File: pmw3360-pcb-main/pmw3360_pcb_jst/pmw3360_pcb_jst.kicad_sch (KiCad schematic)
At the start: 20 parts, among them J1 Conn_01x08, U1 PMW3360DM-T2QU, U2 TLV74318PDBVR

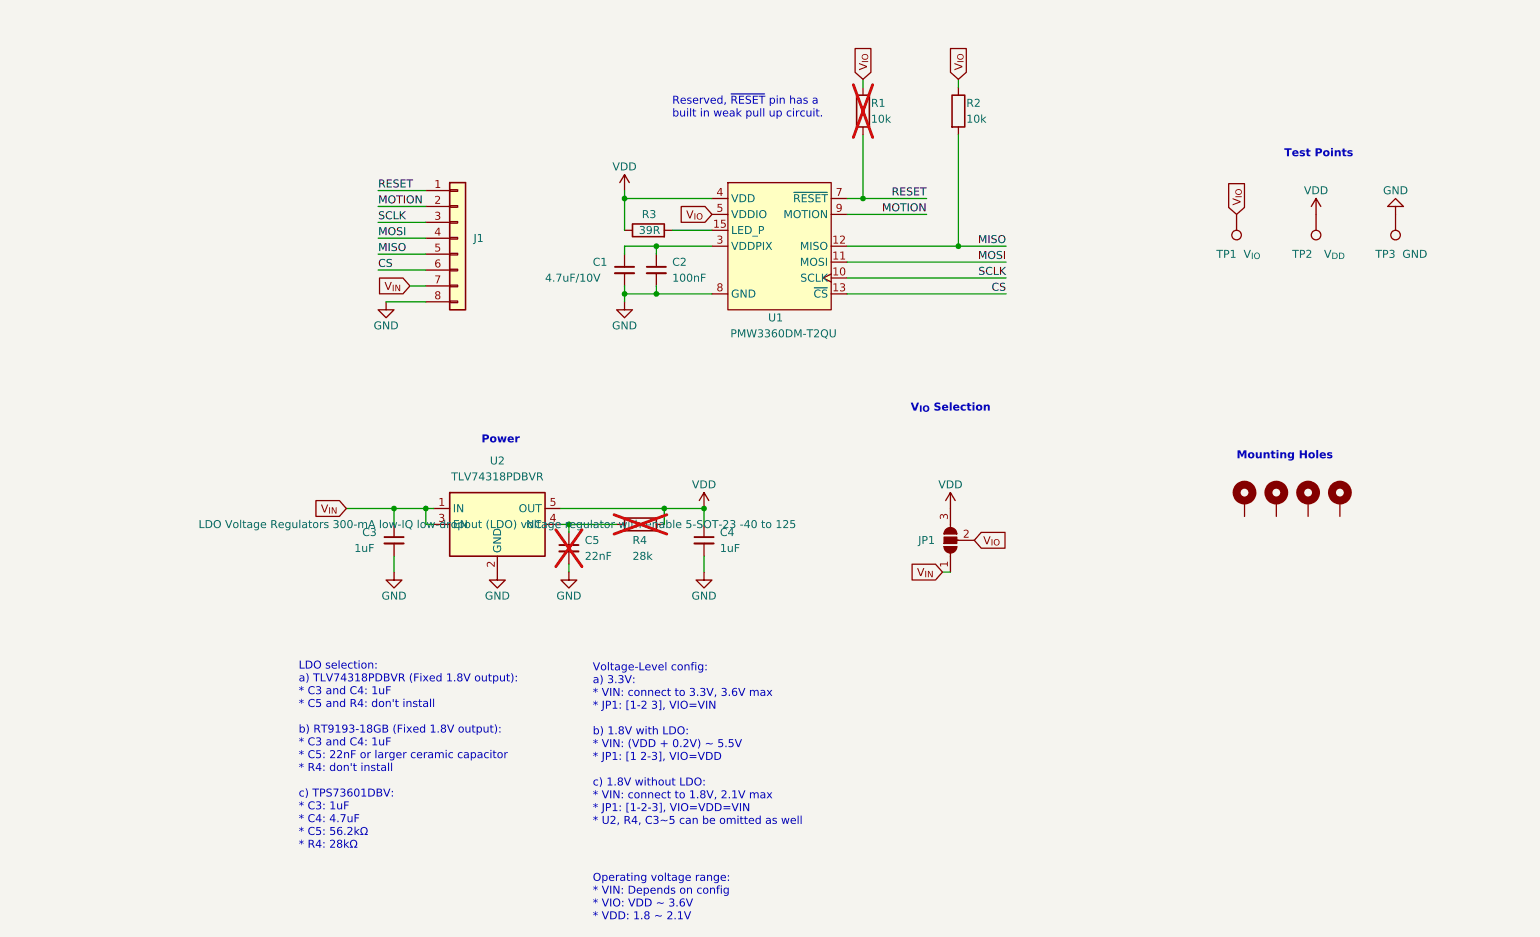
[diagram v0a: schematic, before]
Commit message: mouse sensor bots libraries
- footprints not done yet. shematics yes.
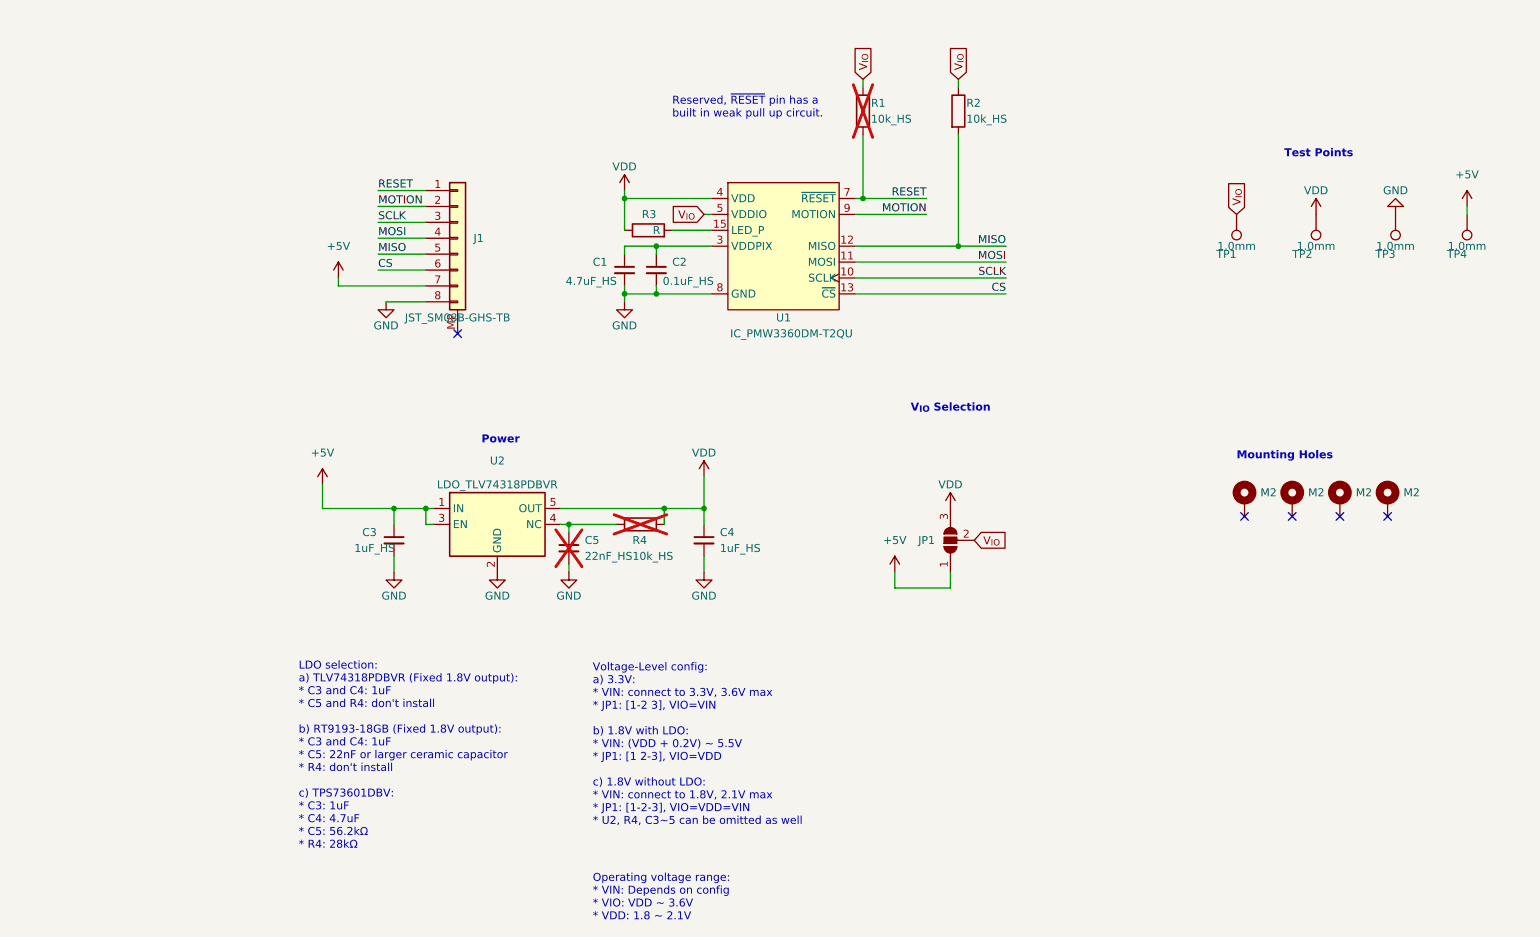
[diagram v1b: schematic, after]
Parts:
- added TP4: 1.0mm, TestPoint:TestPoint_Pad_D1.0mm, symbol bots:TestPoint1.0mm
- C1: value 4.7uF/10V -> 4.7uF_HS; symbol Device:C_Small -> bots:C_4.7uF_HS
- C2: value 100nF -> 0.1uF_HS; symbol Device:C_Small -> bots:C_0.1uF_HS
- C3, C4: value 1uF -> 1uF_HS; symbol Device:C_Small -> bots:C_1uF_HS
- C5: value 22nF -> 22nF_HS; symbol Device:C_Small -> bots:C_22nF_HS; MPN (none) -> CL10B223KB8NNNC; Mfr. # CL10B223KB8NNNC -> (none)
- H1, H2, H3, H4: value MountingHole_Pad -> M2; footprint MountingHole:MountingHole_2.2mm_M2_ISO14580_Pad -> bots:MountingHole_2.2mm_M2_ISO14580_Pad; symbol Mechanical:MountingHole_Pad -> bots:MountingHole_Pad_M2NoThread
- J1: value Conn_01x08 -> JST_SM08B-GHS-TB; symbol Connector_Generic:Conn_01x08 -> bots:JST_SM08B-GHS-TB
- JP1: symbol Jumper:SolderJumper_3_Open -> bots:SolderJumper_3_Open; now left out of the parts list
- R1, R2: value 10k -> 10k_HS; symbol Device:R -> bots:R_10k_HS
- R3: value 39R -> R
- R4: value 28k -> 10k_HS; symbol Device:R -> bots:R_10k_HS
- TP1: value V_{IO} -> 1.0mm; symbol Connector:TestPoint -> bots:TestPoint1.0mm
- TP2: value V_{DD} -> 1.0mm; symbol Connector:TestPoint -> bots:TestPoint1.0mm
- TP3: value GND -> 1.0mm; symbol Connector:TestPoint -> bots:TestPoint1.0mm
- U1: value PMW3360DM-T2QU -> IC_PMW3360DM-T2QU; footprint PMW3360_PCB:PMW3360DM-T2QU 16Pin -> bots:IC_PMW3360DM-T2QU 16Pin; symbol PMW3360_PCB:PMW3360DM-T2QU -> bots:IC_PMW3360DM-T2QU
- U2: value TLV74318PDBVR -> LDO_TLV74318PDBVR; symbol PMW3360_PCB:TLV74318PDBVR -> bots:LDO_TLV74318PDBVR
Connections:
- net V_{IN} renamed +5V
- net +5V: now also TP4.1
- no-connect marks 0 -> 5
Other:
- moved on the sheet: U1

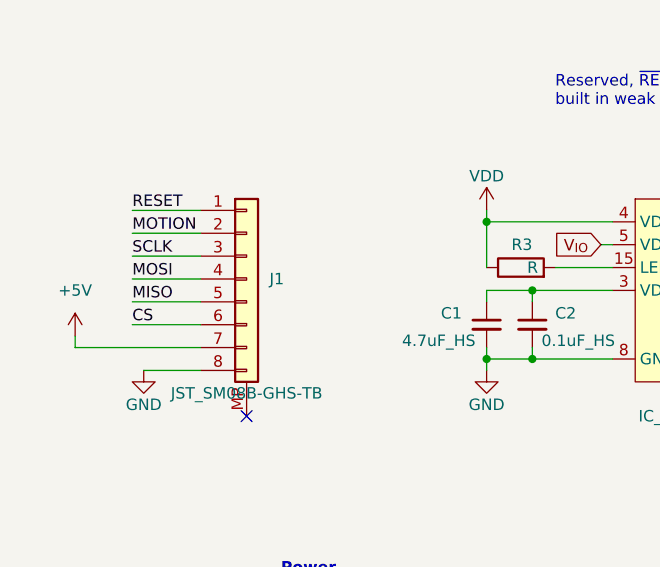
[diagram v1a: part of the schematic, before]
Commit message: 3dmodels + footprints
- one resistor unvalued + no footprint
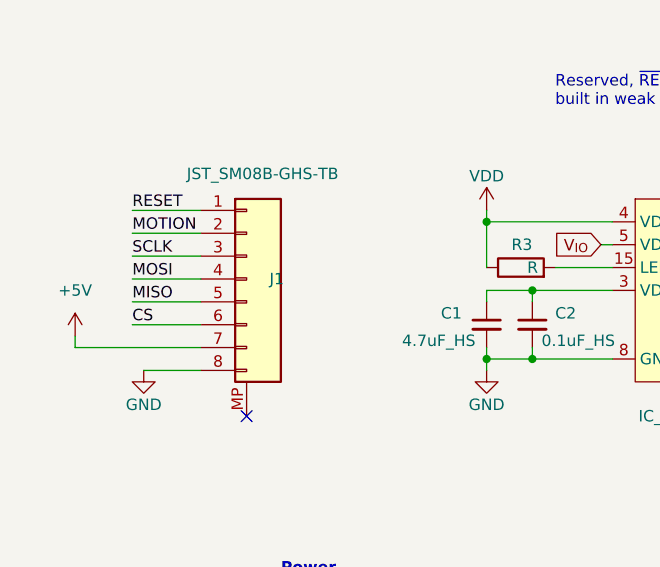
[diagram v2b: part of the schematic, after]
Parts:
- C1, C2, C3, C4, C5: footprint Capacitor_SMD:C_0603_1608Metric_Pad1.08x0.95mm_HandSolder -> bots:C_0603_1608Metric_Pad1.08x0.95mm_HandSolder
- J1: footprint Connector_JST:JST_GH_SM08B-GHS-TB_1x08-1MP_P1.25mm_Horizontal -> bots:JST_GH_SM08B-GHS-TB_1x08-1MP_P1.25mm_Horizontal
- JP1: footprint Jumper:SolderJumper-3_P1.3mm_Open_RoundedPad1.0x1.5mm_NumberLabels -> bots:SolderJumper-3_P1.3mm_Open_RoundedPad1.0x1.5mm_NumberLabels
- R1, R2, R4: footprint Resistor_SMD:R_0603_1608Metric_Pad0.98x0.95mm_HandSolder -> bots:R_0603_1608Metric_Pad0.98x0.95mm_HandSolder
- R3: footprint Resistor_SMD:R_0603_1608Metric_Pad0.98x0.95mm_HandSolder -> (none)
- TP1, TP2, TP3, TP4: footprint TestPoint:TestPoint_Pad_D1.0mm -> bots:TestPoint_Pad_D1.0mm
- U2: LCSC C485152 -> (none); Mfr. # TLV74318PDBVR -> (none)
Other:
- moved on the sheet: J1
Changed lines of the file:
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@@
 			)
 		)
-		(property "Footprint" "TestPoint:TestPoint_Pad_D1.0mm"
+		(property "Footprint" "bots:TestPoint_Pad_D1.0mm"
 			(at 222.25 71.12 0)
 			(effects
@@
 			)
 		)
-		(property "Footprint" "Resistor_SMD:R_0603_1608Metric_Pad0.98x0.95mm_HandSolder"
+		(property "Footprint" "bots:R_0603_1608Metric_Pad0.98x0.95mm_HandSolder"
 			(at 119.38 118.872 90)
 			(effects
@@
 			)
 		)
-		(property "Footprint" "Capacitor_SMD:C_0603_1608Metric_Pad1.08x0.95mm_HandSolder"
+		(property "Footprint" "bots:C_0603_1608Metric_Pad1.08x0.95mm_HandSolder"
 			(at 129.54 123.19 0)
 			(effects
@@
 			)
 		)
-		(property "Footprint" "Resistor_SMD:R_0603_1608Metric_Pad0.98x0.95mm_HandSolder"
+		(property "Footprint" ""
 			(at 120.65 75.438 90)
 			(effects
@@
 			)
 		)
-		(property "Footprint" "Capacitor_SMD:C_0603_1608Metric_Pad1.08x0.95mm_HandSolder"
+		(property "Footprint" "bots:C_0603_1608Metric_Pad1.08x0.95mm_HandSolder"
 			(at 116.84 80.01 0)
 			(effects
@@
 			)
 		)
-		(property "Footprint" "Capacitor_SMD:C_0603_1608Metric_Pad1.08x0.95mm_HandSolder"
+		(property "Footprint" "bots:C_0603_1608Metric_Pad1.08x0.95mm_HandSolder"
 			(at 107.95 124.46 0)
 			(effects
@@
 			)
 		)
-		(property "Footprint" "TestPoint:TestPoint_Pad_D1.0mm"
+		(property "Footprint" "bots:TestPoint_Pad_D1.0mm"
 			(at 246.38 71.12 0)
 			(effects
@@
 			)
 		)
-		(property "Footprint" "Capacitor_SMD:C_0603_1608Metric_Pad1.08x0.95mm_HandSolder"
+		(property "Footprint" "bots:C_0603_1608Metric_Pad1.08x0.95mm_HandSolder"
 			(at 80.01 123.19 0)
 			(effects
@@
 			)
 		)
-		(property "Footprint" "Resistor_SMD:R_0603_1608Metric_Pad0.98x0.95mm_HandSolder"
+		(property "Footprint" "bots:R_0603_1608Metric_Pad0.98x0.95mm_HandSolder"
 			(at 153.162 54.61 90)
 			(effects
@@
 			)
 		)
-		(property "Footprint" "Capacitor_SMD:C_0603_1608Metric_Pad1.08x0.95mm_HandSolder"
+		(property "Footprint" "bots:C_0603_1608Metric_Pad1.08x0.95mm_HandSolder"
 			(at 121.92 80.01 0)
 			(effects
@@
 			)
 		)
-		(property "Footprint" "TestPoint:TestPoint_Pad_D1.0mm"
+		(property "Footprint" "bots:TestPoint_Pad_D1.0mm"
 			(at 234.95 71.12 0)
 			(effects
@@
 			)
 		)
-		(property "Footprint" "Resistor_SMD:R_0603_1608Metric_Pad0.98x0.95mm_HandSolder"
+		(property "Footprint" "bots:R_0603_1608Metric_Pad0.98x0.95mm_HandSolder"
 			(at 168.402 54.61 90)
 			(effects
@@
 			)
 		)
-		(property "Footprint" "Jumper:SolderJumper-3_P1.3mm_Open_RoundedPad1.0x1.5mm_NumberLabels"
+		(property "Footprint" "bots:SolderJumper-3_P1.3mm_Open_RoundedPad1.0x1.5mm_NumberLabels"
 			(at 168.91 123.19 0)
 			(effects
@@
 			)
 		)
-		(property "LCSC" "C485152"
-			(at 96.52 120.65 0)
-			(effects
-				(font
-					(size 1.27 1.27)
-				)
-				(hide yes)
-			)
-		)
-		(property "Mfr. #" "TLV74318PDBVR"
-			(at 96.52 120.65 0)
-			(effects
-				(font
-					(size 1.27 1.27)
-				)
-				(hide yes)
-			)
-		)
 		(pin "1"
 		)
@@
 		)
 		(property "Value" "JST_SM08B-GHS-TB"
-			(at 90.17 87.63 0)
-			(effects
-				(font
-					(size 1.27 1.27)
-				)
-			)
-		)
-		(property "Footprint" "Connector_JST:JST_GH_SM08B-GHS-TB_1x08-1MP_P1.25mm_Horizontal"
+			(at 91.948 63.246 0)
+			(effects
+				(font
+					(size 1.27 1.27)
+				)
+			)
+		)
+		(property "Footprint" "bots:JST_GH_SM08B-GHS-TB_1x08-1MP_P1.25mm_Horizontal"
 			(at 90.17 74.93 0)
 			(effects
@@
 			)
 		)
-		(property "Footprint" "TestPoint:TestPoint_Pad_D1.0mm"
+		(property "Footprint" "bots:TestPoint_Pad_D1.0mm"
 			(at 209.55 71.12 0)
 			(effects

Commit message: libraries and stuff
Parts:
- R3: value R -> 39R_HS; footprint (none) -> bots:R_0603_1608Metric_Pad0.98x0.95mm_HandSolder; symbol Device:R -> bots:R_39R_HS
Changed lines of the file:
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@@
 	(text "V_{IO} Selection"
 		(exclude_from_sim no)
-		(at 162.56 102.87 0)
+		(at 163.322 108.458 0)
 		(effects
 			(font
@@
 	)
 	(symbol
-		(lib_id "Device:R")
+		(lib_id "bots:R_39R_HS")
 		(at 120.65 73.66 90)
 		(unit 1)
@@
 			)
 		)
-		(property "Value" "R"
-			(at 122.555 73.66 90)
+		(property "Value" "39R_HS"
+			(at 116.586 74.676 90)
 			(effects
 				(font
@@
 			)
 		)
-		(property "Footprint" ""
+		(property "Footprint" "bots:R_0603_1608Metric_Pad0.98x0.95mm_HandSolder"
 			(at 120.65 75.438 90)
 			(effects

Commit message: mouse_sensorV1 prod done
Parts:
- J1: value JST_SM08B-GHS-TB -> JST_BM08B-GHS-TBT; footprint bots:JST_GH_SM08B-GHS-TB_1x08-1MP_P1.25mm_Horizontal -> bots:JST_BM08B-GHS-TBT_LF__SN__N_; symbol bots:JST_SM08B-GHS-TB -> bots:JST_BM08B-GHS-TBT
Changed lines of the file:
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@@
 	)
 	(symbol
-		(lib_id "bots:JST_SM08B-GHS-TB")
+		(lib_id "bots:JST_BM08B-GHS-TBT")
 		(at 90.17 74.93 0)
 		(unit 1)
@@
 			)
 		)
-		(property "Value" "JST_SM08B-GHS-TB"
-			(at 91.948 63.246 0)
+		(property "Value" "JST_BM08B-GHS-TBT"
+			(at 92.71 92.202 0)
 			(effects
 				(font
@@
 			)
 		)
-		(property "Footprint" "bots:JST_GH_SM08B-GHS-TB_1x08-1MP_P1.25mm_Horizontal"
+		(property "Footprint" "bots:JST_BM08B-GHS-TBT_LF__SN__N_"
 			(at 90.17 74.93 0)
 			(effects

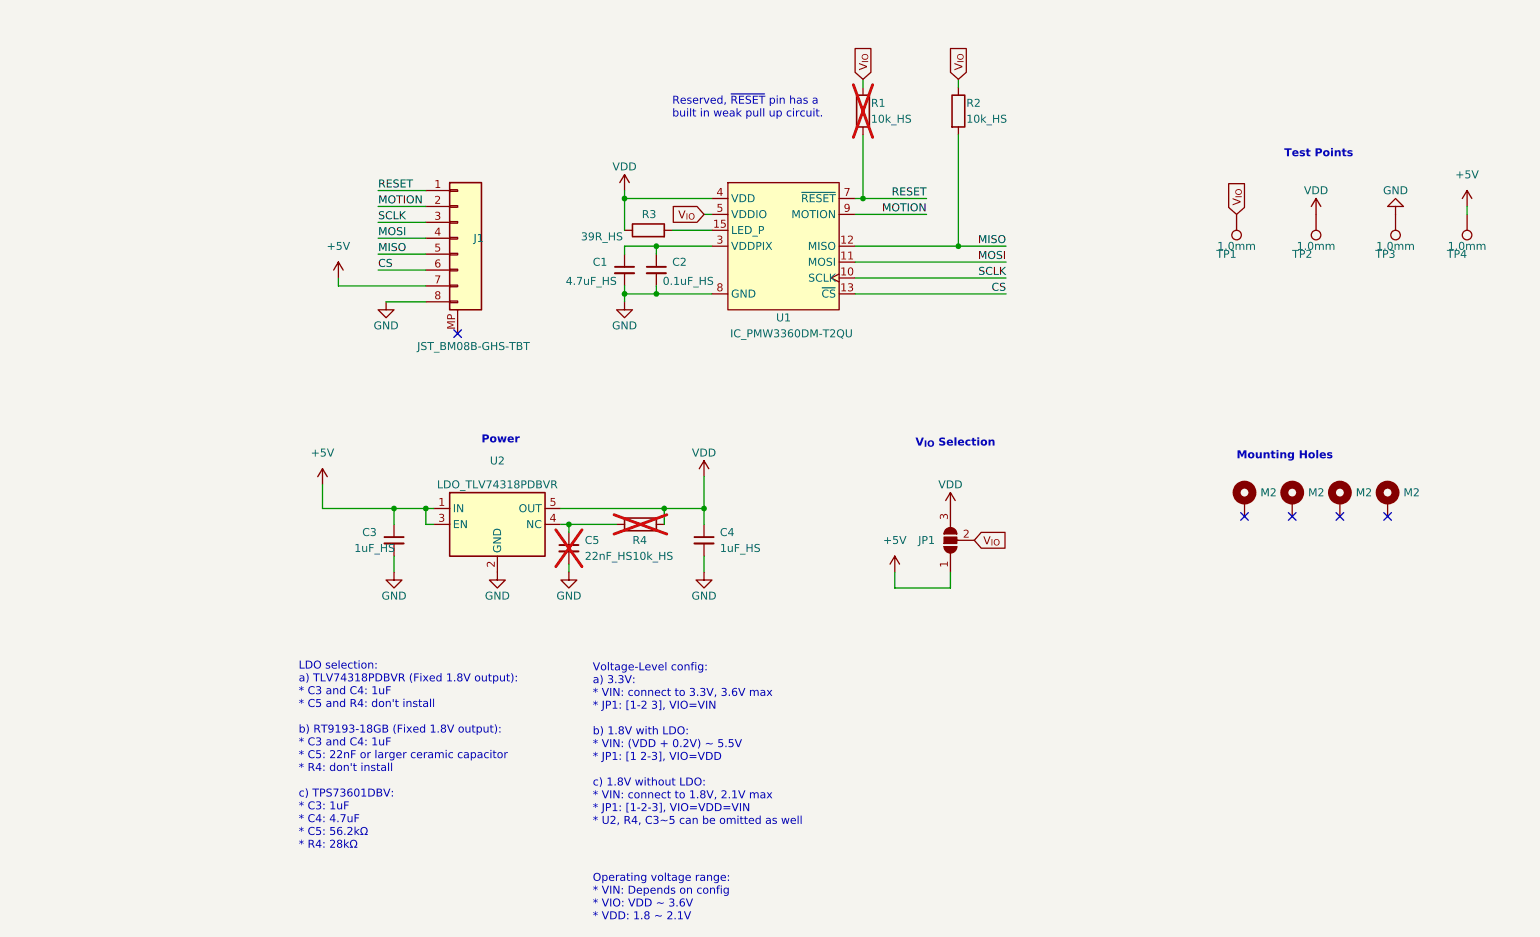
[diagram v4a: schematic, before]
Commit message: production files - working
- modified board slightly, added 3d models, added part numbers for JLC
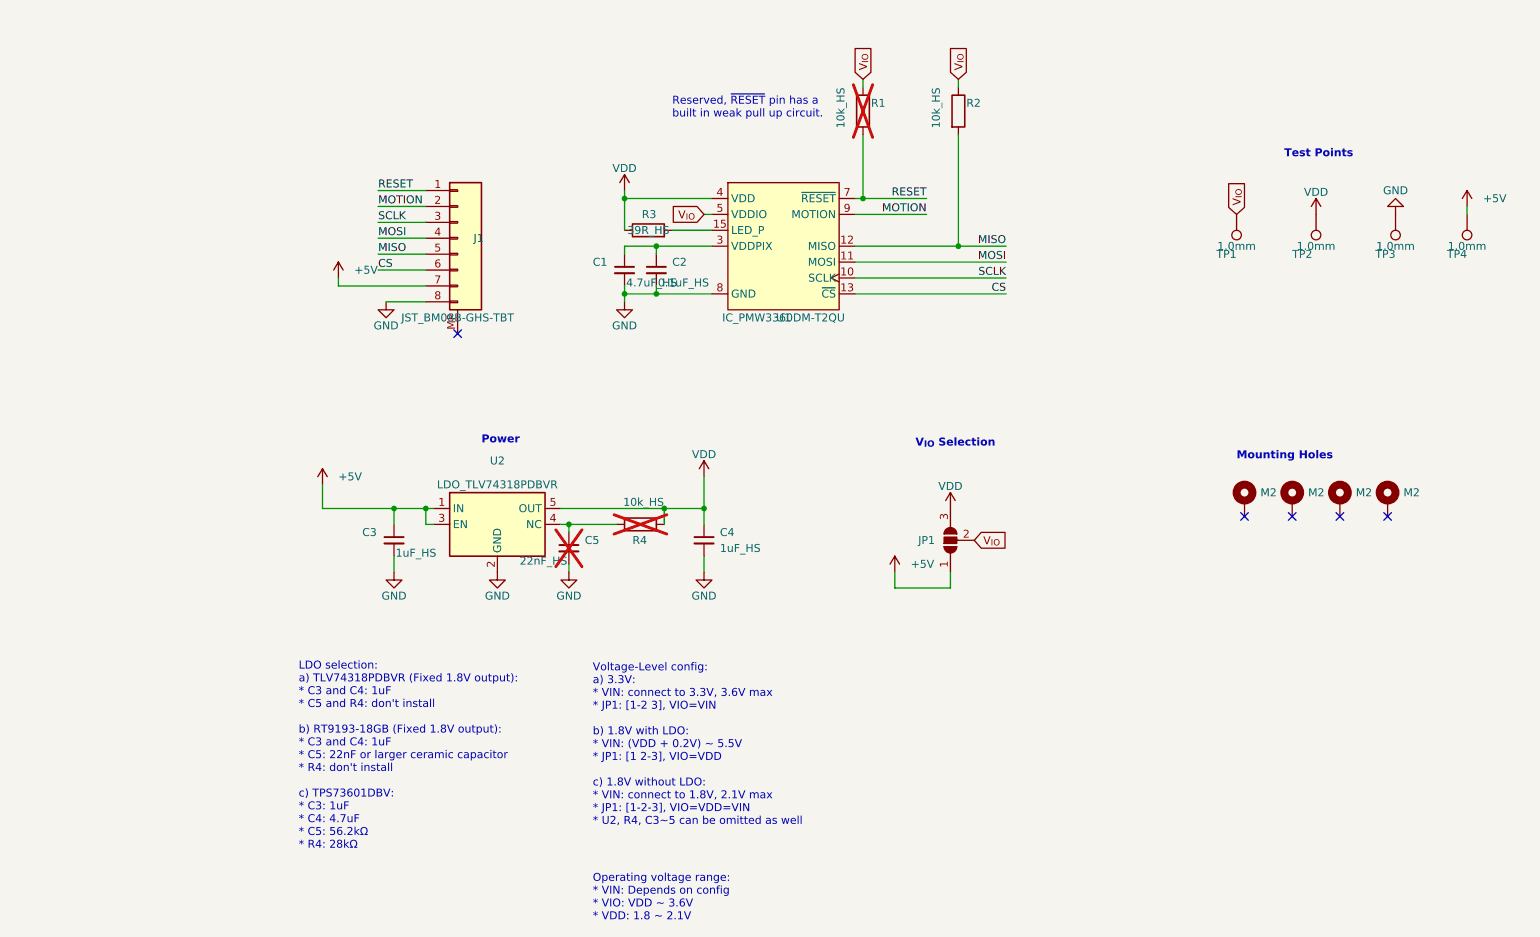
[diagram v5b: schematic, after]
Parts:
- C1: LCSC (none) -> C19666; MPN (none) -> CL10A475KO8NNNC
- C2: LCSC (none) -> C14663; MPN (none) -> CC0603KRX7R9BB104
- C3, C4: LCSC (none) -> C15849; MPN (none) -> CL10A105KB8NNNC
- J1: LCSC (none) -> C133062; MPN (none) -> BM08B-GHS-TBT(LF)(SN)
- R1, R2, R4: LCSC (none) -> C25804; MPN (none) -> 0603WAF1002T5E
- R3: Extended (none) -> Yes; LCSC (none) -> C23154; MPN (none) -> 0603WAF390JT5E
- U1: LCSC (none) -> C20612443; MPN (none) -> PMW3360DM-T2QU
- U2: LCSC (none) -> C485152; MPN (none) -> TLV74318PDBVR
